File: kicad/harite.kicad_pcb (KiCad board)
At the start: 2 copper layers, 258.2 x 95.8 mm, 80 parts, among them J1 503480-0500, J2 Wired Joystick, J4 5034801200, J5 5034801200, U1 RP2040_Zero, U2 RP2040_Zero

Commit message: Change to ps5 joystick
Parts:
- removed D31, D32, D33, D34, D35, D36, D37, D38, D39, D40, D41, D42, D43, D44, D45, D46, D47, D48, D49, D50: D, ScottoKeebs_Components:Diode_SOD-123
- removed the G*** at (175.2, 115.3)
- removed H10, H6, H7, H8, H9: Mounting_Hole, MountingHole:MountingHole_2.2mm_M2_Pad_Via
- removed S10, S7, S8, S9: SKRHADE010, footprints:SKRHADE
- removed U2: RP2040_Zero, ScottoKeebs_MCU:RP2040_Zero
- removed USB2: HRO-TYPE-C-31-M-12, footprints:HRO-TYPE-C-31-M-12
- added J3: 59453-051110ECHLF, footprints:AMPHENOL_59453-051110ECHLF, F.Cu at (123.7, 106.0)
- J1: value 503480-0500 -> 59453-121110ECHLF; footprint footprints:5034800540 -> footprints:AMPHENOL_59453-121110ECHLF
- J2: value Wired Joystick -> 59453-051110ECHLF; footprint footprints:Wired-Joystick -> footprints:AMPHENOL_59453-051110ECHLF
- J4, J5: value 5034801200 -> 59453-081110EDHLF; footprint footprints:5034801200 -> footprints:AMPHENOL_59453-081110EDHLF
- S1, S2, S3, S4, S5, S6: footprint footprints:SKRHADE -> footprints:SKRHADE010
- moved D30 151.2 mm to (138.3, 160.5), turned to 0 degrees
- moved S6 142.6 mm to (133.0, 149.0), turned to -45 degrees
- moved D29 142.5 mm to (143.8, 155.0), turned to 0 degrees
- moved D26 141.0 mm to (116.3, 97.5), turned to 0 degrees
- moved D28 125.7 mm to (139.0, 133.3), turned to 0 degrees
- moved D27 123.5 mm to (139.0, 130.0), turned to 0 degrees
- moved J1 74.0 mm to (81.8, 89.7)
- moved D24 57.5 mm to (117.8, 145.5), turned to 0 degrees
- moved D23 52.7 mm to (118.3, 142.0), turned to 0 degrees
- moved D22 52.4 mm to (124.8, 142.0), turned to 0 degrees
- moved D21 38.0 mm to (116.3, 125.5), turned to 0 degrees
- moved J2 31.7 mm to (124.8, 97.0), turned to 180 degrees
- moved D20 25.9 mm to (119.5, 120.0), turned to 0 degrees
- moved D19 24.0 mm to (122.8, 115.0), turned to 0 degrees
- moved D25 17.2 mm to (116.8, 89.5), turned to 0 degrees
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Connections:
- D19 pad 1: Row 4 -> Row 1
- D20 pad 1: Row 5 -> Row 2
- D21 pad 1: Row 1 -> Row 3
- D22 pad 1: Row 2 -> Row 1
- D23 pad 1: Row 3 -> Row 2
- D24 pad 1: Row 4 -> Row 3
- D25 pad 1: Row 5 -> Row 4
- D26 pad 1: RRow 1 -> Row 5
- D27 pad 1: RRow 2 -> Row 4
- D28 pad 1: RRow 3 -> Row 5
- D29 pad 1: RRow 4 -> Row 4
- D30 pad 1: RRow 5 -> Row 5
- J1 pad 1: E3V3 -> unconnected-(J1-Pad1)
- J1 pad 2: EJY -> unconnected-(J1-Pad2)
- J1 pad 3: EJC -> unconnected-(J1-Pad3)
- J1 pad 4: EGND -> unconnected-(J1-Pad4)
- J1 pad 5: EJX -> unconnected-(J1-Pad5)
- J2 pad 1: E3V3 -> 3V3
- J2 pad 2: EJY -> JY
- J2 pad 3: EJC -> JC
- J2 pad 4: EGND -> GND
- J2 pad 5: EJX -> JX
- J4 pad 1: EJX -> ERow 5
- J4 pad 2: EGND -> ECol 5
- J4 pad 3: EJC -> ERow 4
- J4 pad 4: EJY -> ERow 1
- J4 pad 5: E3V3 -> ERow 2
- J4 pad 6: unconnected-(J4-Pad6) -> ERow 3
- J4 pad 7: ERow 5 -> unconnected-(J4-Pad7)
- J4 pad 8: ECol 5 -> unconnected-(J4-Pad8)
- J5 pad 1: Net-(D23-A) -> unconnected-(J5-Pad1)
- J5 pad 2: Net-(D22-A) -> unconnected-(J5-Pad2)
- J5 pad 3: Net-(D21-A) -> Row 3
- J5 pad 4: Net-(D24-A) -> Row 2
- J5 pad 5: Col 5 -> Row 1
- J5 pad 6: Net-(D25-A) -> Row 4
- J5 pad 7: unconnected-(J5-Pad7) -> Col 5
- J5 pad 8: 3V3 -> Row 5
- S4 pad 4: Net-(D19-A) -> Net-(D25-A)
- S4 pad 6: Net-(D20-A) -> Net-(D26-A)
- S5 pad 1: ERow 1 -> Net-(D19-A)
- S5 pad 2: ERow 2 -> Net-(D20-A)
- S5 pad 3: ERow 3 -> Net-(D21-A)
- S5 pad 4: ERow 4 -> Net-(D27-A)
- S5 pad 5: ECol 5 -> Col 5
- S5 pad 6: ERow 5 -> Net-(D28-A)
- S6 pad 1: Net-(D26-A) -> Net-(D22-A)
- S6 pad 2: Net-(D27-A) -> Net-(D23-A)
- S6 pad 3: Net-(D28-A) -> Net-(D24-A)
- S6 pad 5: RCol 1 -> Col 6
- U1 pad 10: Col 1 -> Row 4
- U1 pad 11: Col 2 -> Row 5
- U1 pad 12: Col 3 -> Col 1
- U1 pad 13: Col 4 -> Col 2
- U1 pad 14: Col 5 -> Col 3
- U1 pad 15: unconnected-(U1-14-Pad15) -> Col 4
- U1 pad 16: unconnected-(U1-15-Pad16) -> Col 5
- U1 pad 17: JX -> Col 6
- U1 pad 18: JY -> JX
- U1 pad 19: JC -> JY
- U1 pad 20: unconnected-(U1-29-Pad20) -> JC
- U1 pad 3: unconnected-(U1-2-Pad3) -> SCK
- U1 pad 4: unconnected-(U1-3-Pad4) -> MOSI
- U1 pad 5: Row 1 -> MISO
- U1 pad 6: Row 2 -> SS
- U1 pad 7: Row 3 -> Row 1
- U1 pad 8: Row 4 -> Row 2
- U1 pad 9: Row 5 -> Row 3
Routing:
- net EJX: track 24.6 -> 0.00 mm
- net EGND: track 23.5 -> 0.00 mm
- net EJC: track 22.5 -> 0.00 mm
- net EJY: track 21.6 -> 0.00 mm
- net ERow 5: track 21.3 -> 0.00 mm
- net E3V3: track 20.0 -> 0.00 mm
- net ECol 5: track 19.2 -> 0.00 mm
- net ERow 4: track 16.7 -> 0.00 mm
- net Col 5: track 14.5 -> 0.00 mm, vias 2 -> 0
- net ERow 3: track 10.2 -> 0.00 mm
- net ERow 2: track 8.53 -> 0.00 mm
- net Net-(D25-A): track 7.33 -> 0.00 mm
- net ERow 1: track 7.11 -> 0.00 mm
- net Net-(D23-A): track 5.66 -> 0.00 mm
- net Net-(D24-A): track 5.62 -> 0.00 mm
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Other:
- board size 258.2 x 95.8 mm -> 126 x 76.7 mm
- board text removed: "Cirque"
- board text removed: "GND"
- board text removed: "SCK"
- board text removed: "SI"
- board text removed: "SO"
- board text removed: "SS"
- board text removed: "VDD"

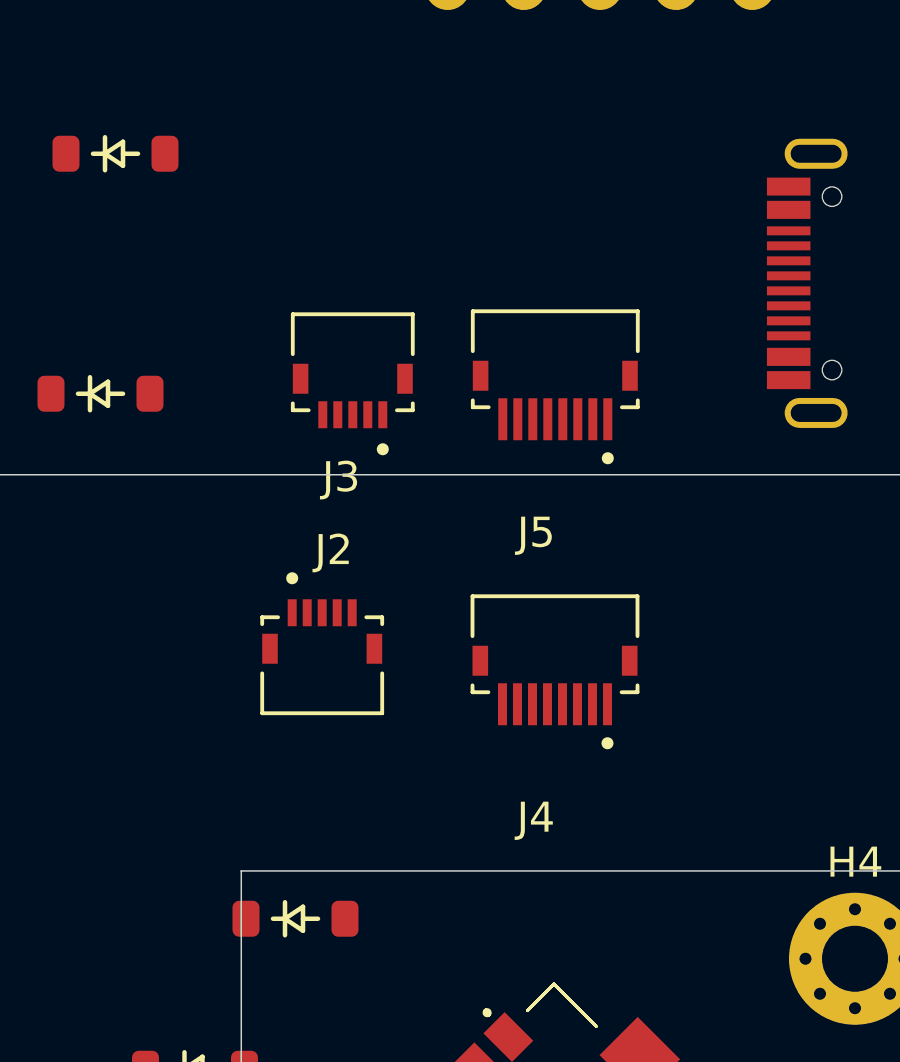
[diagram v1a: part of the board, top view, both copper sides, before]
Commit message: fix footprints
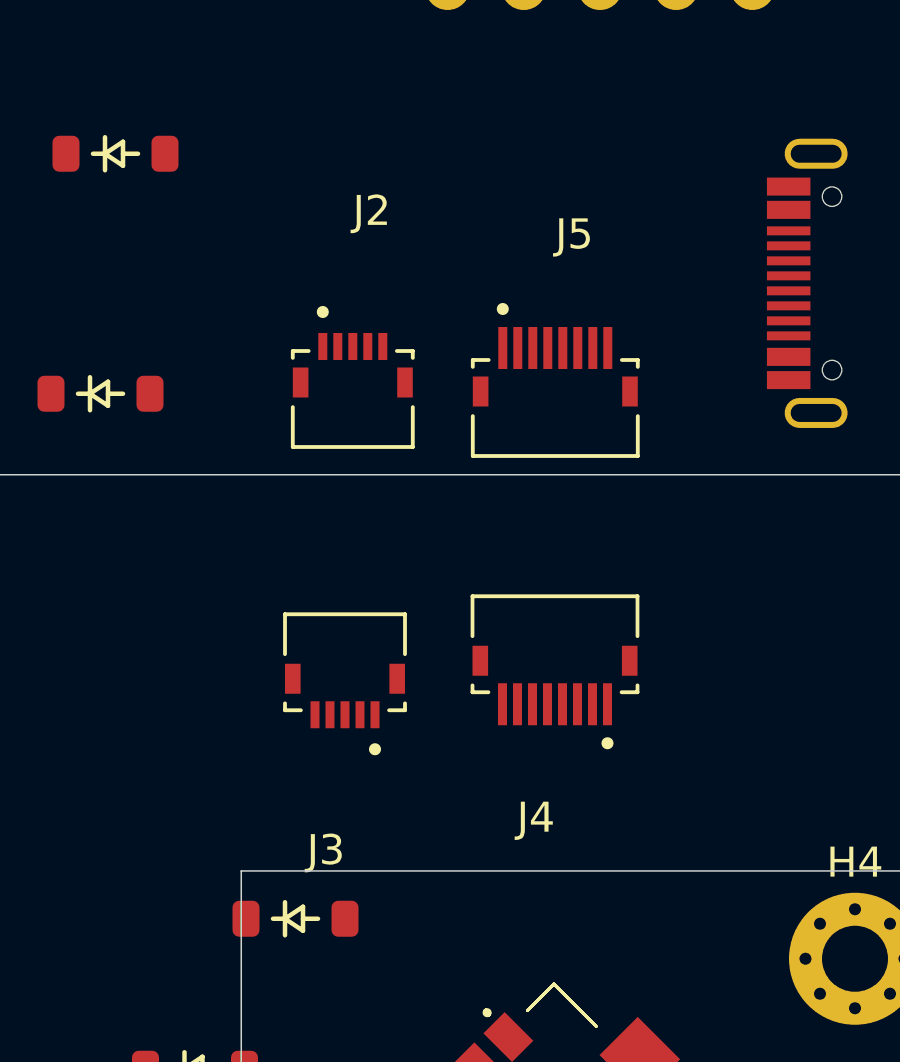
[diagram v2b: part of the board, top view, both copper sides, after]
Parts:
- moved J5 1.33 mm to (131.5, 97.8), turned to 0 degrees
- moved J3 1.26 mm to (124.5, 107.0), turned to 180 degrees
- moved J2 0.12 mm to (124.8, 97.1), turned to 0 degrees

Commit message: Update nets
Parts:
- moved J3 19.5 mm to (105.0, 106.5)
- moved H5 13.4 mm to (122.8, 148.2)
- moved D30 13.1 mm to (135.7, 147.7), turned to 135 degrees
- moved D29 11.2 mm to (137.7, 145.7), turned to 135 degrees
- moved D24 10.5 mm to (124.2, 137.2), turned to -45 degrees
- moved D23 10.4 mm to (126.2, 135.2), turned to -45 degrees
- moved D21 9.68 mm to (123.7, 119.2), turned to -45 degrees
- moved D22 9.44 mm to (128.2, 133.2), turned to -45 degrees
- moved H3 8.67 mm to (119.3, 97.2)
- moved H4 8.18 mm to (139.2, 108.5)
- moved S6 8.15 mm to (131.5, 141.0)
- moved D20 6.79 mm to (125.7, 117.2), turned to -45 degrees
- moved D26 5.91 mm to (111.2, 94.7), turned to 135 degrees
- moved D28 5.47 mm to (136.2, 128.7), turned to 135 degrees
- moved D5 5.40 mm to (36.2, 102.7), turned to 135 degrees
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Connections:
- D19 pad 1: Row 1 -> ERow 1
- D20 pad 1: Row 2 -> ERow 2
- D21 pad 1: Row 3 -> ERow 3
- D22 pad 1: Row 1 -> ERow 1
- D23 pad 1: Row 2 -> ERow 2
- D24 pad 1: Row 3 -> ERow 3
- D27 pad 1: Row 4 -> ERow 4
- D28 pad 1: Row 5 -> ERow 5
- D29 pad 1: Row 4 -> ERow 4
- D30 pad 1: Row 5 -> ERow 5
- J1 pad 1: unconnected-(J1-Pad1) -> 3V3
- J1 pad 10: unconnected-(J1-Pad10) -> SS
- J1 pad 11: unconnected-(J1-Pad11) -> MISO
- J1 pad 12: unconnected-(J1-Pad12) -> SCK
- J1 pad 2: unconnected-(J1-Pad2) -> GND
- J1 pad 8: unconnected-(J1-Pad8) -> MOSI
- J4 pad 7: unconnected-(J4-Pad7) -> ECol 6
- J5 pad 2: unconnected-(J5-Pad2) -> Col 6
- S5 pad 5: Col 5 -> ECol 5
- S6 pad 5: Col 6 -> ECol 6
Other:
- board size 126 x 76.7 mm -> 126 x 90.1 mm

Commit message: routing
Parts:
- moved H2 20.5 mm to (115.0, 64.5)
- moved J1 15.0 mm to (93.5, 89.7)
- moved J2 0.45 mm to (125.0, 97.5)
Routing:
- net Row 3: track 0.00 -> 184.0 mm, vias 0 -> 8
- net Row 2: track 0.00 -> 170.7 mm, vias 0 -> 10
- net Row 1: track 0.00 -> 142.5 mm, vias 0 -> 2
- net Col 1: track 0.00 -> 125.8 mm, vias 0 -> 4
- net Col 2: track 0.00 -> 95.2 mm, vias 0 -> 4
- net 3V3: track 0.00 -> 83.4 mm, vias 0 -> 4
- net SCK: track 0.00 -> 64.4 mm, vias 0 -> 2
- net Col 3: track 0.00 -> 64.3 mm, vias 0 -> 3
- net MOSI: track 0.00 -> 63.8 mm, vias 0 -> 2
- net 5V: track 0.00 -> 63.4 mm
- net MISO: track 0.00 -> 61.9 mm, vias 0 -> 2
- net SS: track 0.00 -> 61.1 mm, vias 0 -> 2
- net GP0: track 0.00 -> 44.3 mm, vias 0 -> 1
- net GP1: track 0.00 -> 39.9 mm, vias 0 -> 3
- net JC: track 0.00 -> 31.4 mm, vias 0 -> 1
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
